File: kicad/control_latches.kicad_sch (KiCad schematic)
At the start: 5 parts, among them U11 7406, U6 74LS374, U7 74LS374, U8 74LS04, U9 74LS08

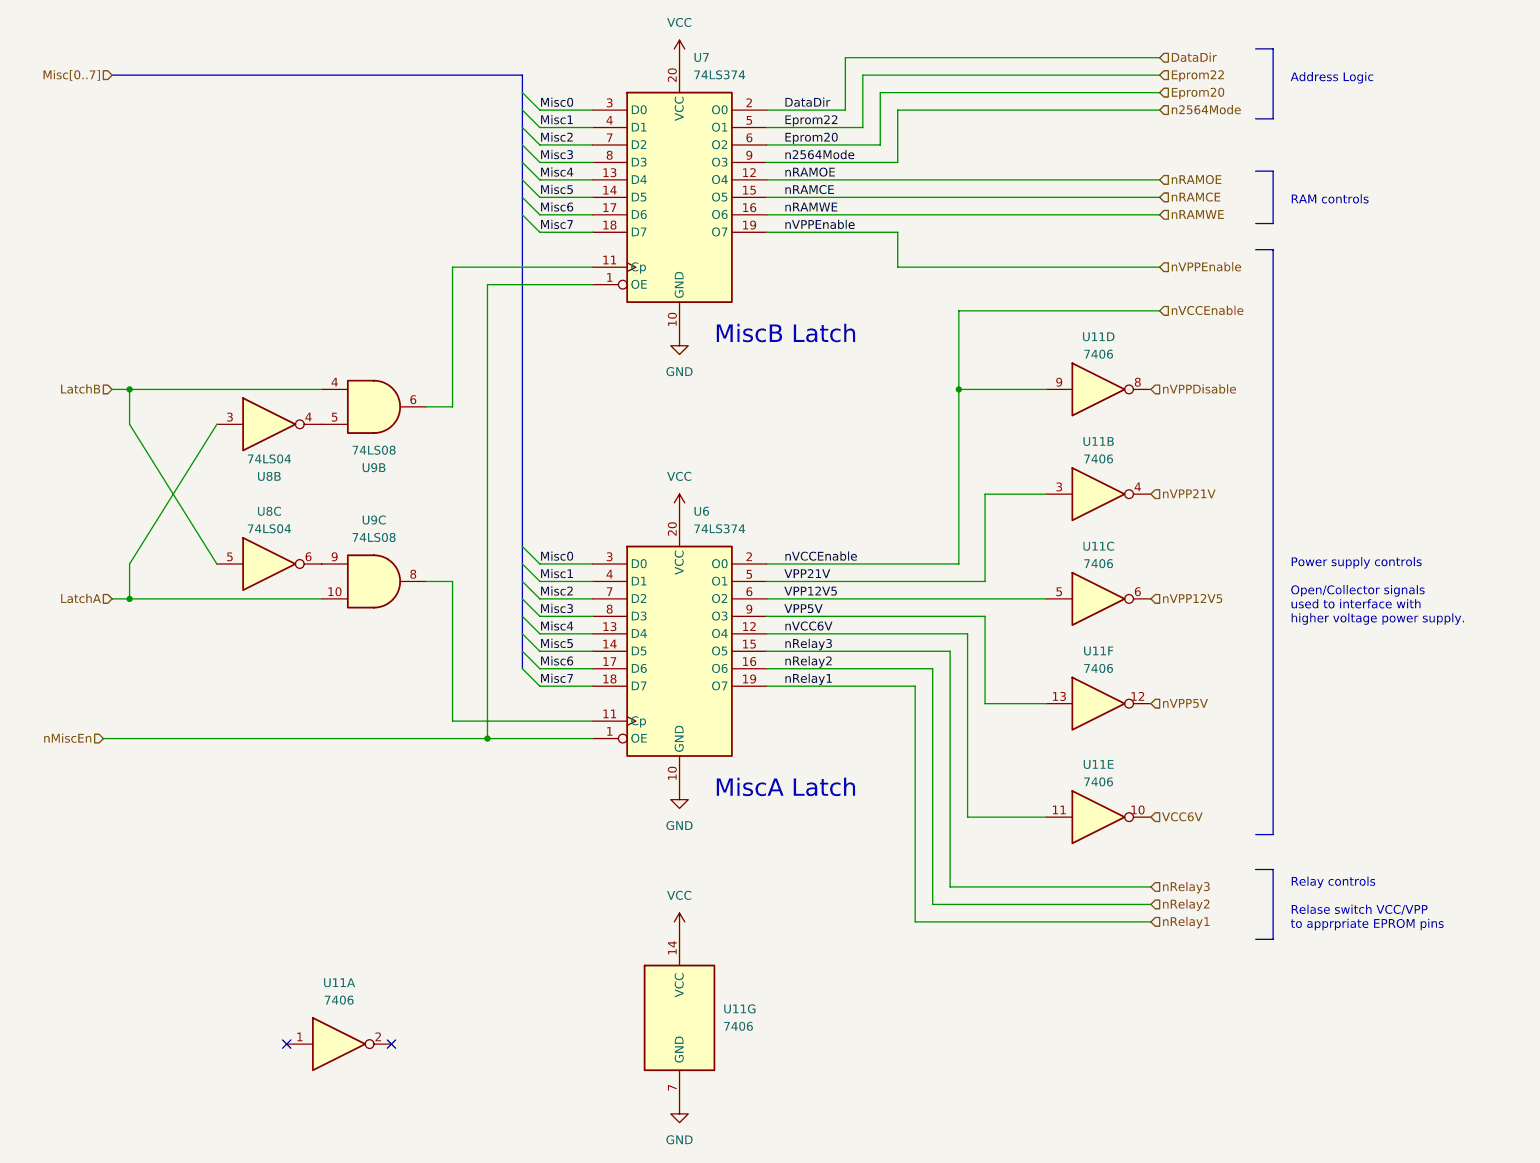
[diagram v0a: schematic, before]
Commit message: Move 7406 onto PSU sheet
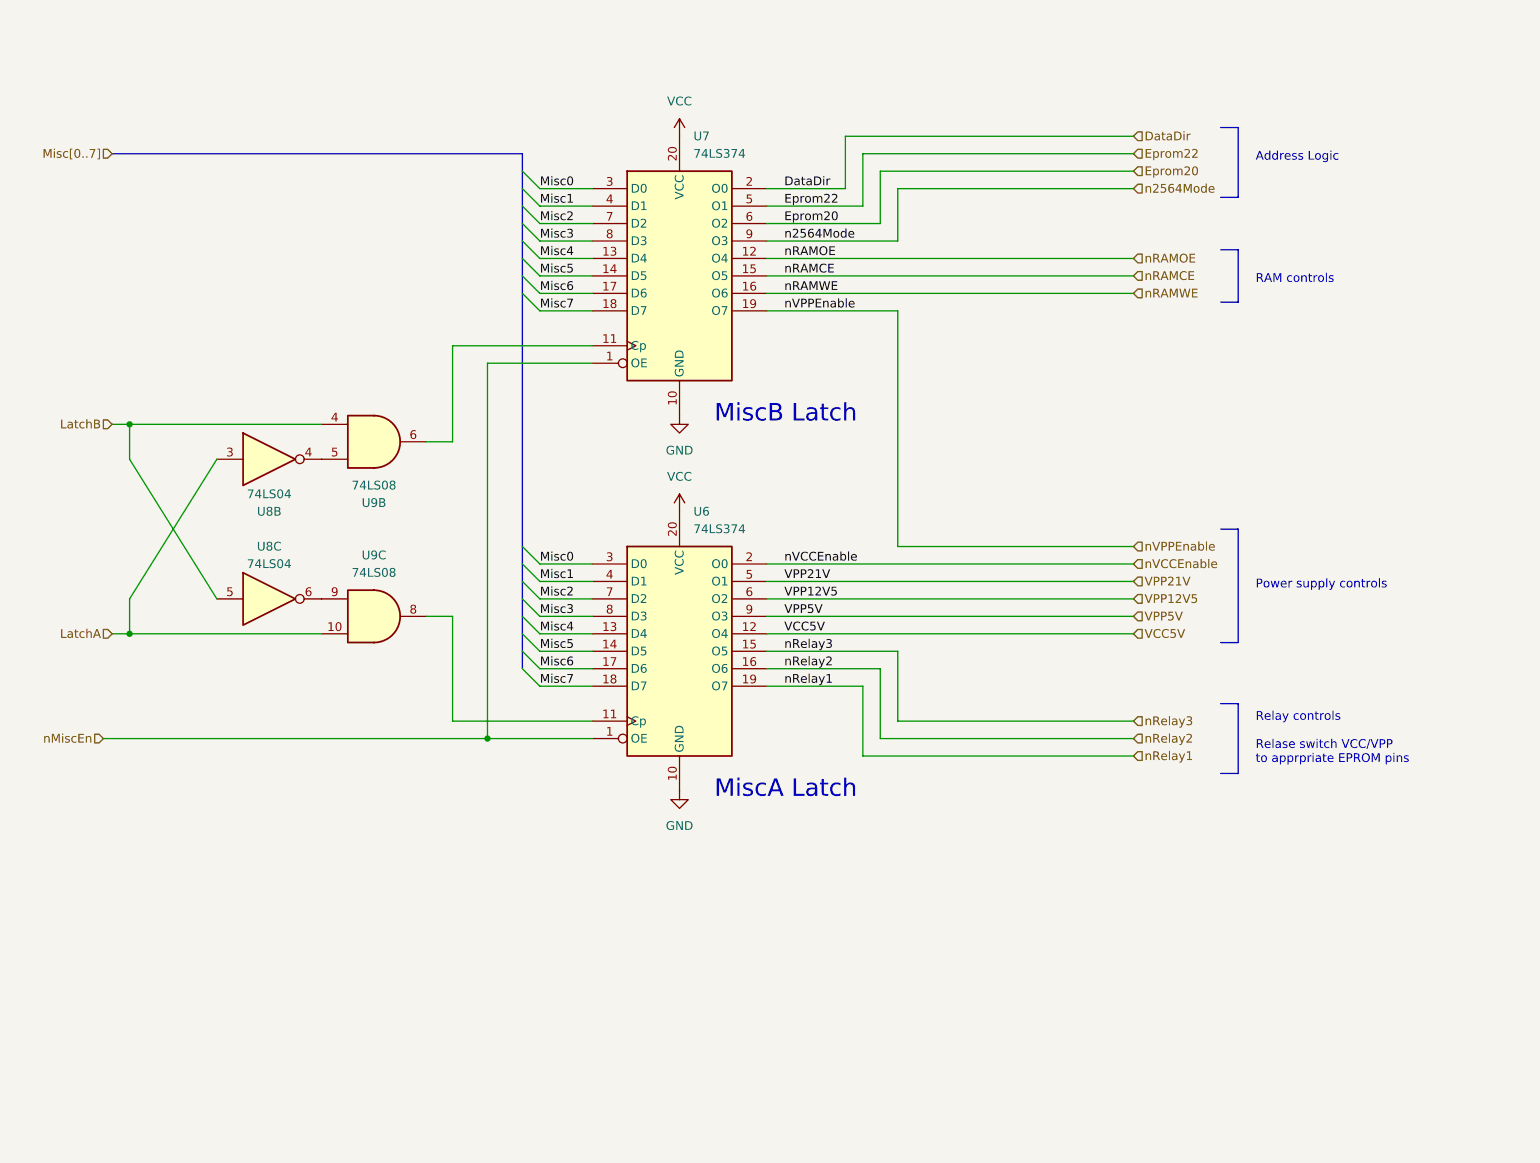
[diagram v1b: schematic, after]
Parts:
- removed U11: 7406, symbol 74xx:74LS06
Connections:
- net nVCC6V renamed VCC5V
- no-connect marks 2 -> 0
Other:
- note added: "Power supply controls"
- note removed: "Power supply controls Open/Collector signals used to interface with higher voltage power supply."
- moved on the sheet: U7, U8B, U8C, U9B, U9C

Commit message: KiCAD: Initial PCB placement
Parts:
- U6, U7: footprint (none) -> Package_DIP:DIP-20_W7.62mm_LongPads
- U8, U9: footprint (none) -> Package_DIP:DIP-14_W7.62mm_LongPads
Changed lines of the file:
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@@
     (property "Reference" "U8" (id 0) (at 90.17 97.79 0))
     (property "Value" "74LS04" (id 1) (at 90.17 100.33 0))
-    (property "Footprint" "" (id 2) (at 90.17 105.41 0)
+    (property "Footprint" "Package_DIP:DIP-14_W7.62mm_LongPads" (id 2) (at 90.17 105.41 0)
       (effects (font (size 1.27 1.27)) hide)
     )
@@
     (property "Reference" "U9" (id 0) (at 105.41 99.06 0))
     (property "Value" "74LS08" (id 1) (at 105.41 101.6 0))
-    (property "Footprint" "" (id 2) (at 105.41 107.95 0)
+    (property "Footprint" "Package_DIP:DIP-14_W7.62mm_LongPads" (id 2) (at 105.41 107.95 0)
       (effects (font (size 1.27 1.27)) hide)
     )
@@
     (property "Reference" "U8" (id 0) (at 90.17 92.71 0))
     (property "Value" "74LS04" (id 1) (at 90.17 90.17 0))
-    (property "Footprint" "" (id 2) (at 90.17 85.09 0)
+    (property "Footprint" "Package_DIP:DIP-14_W7.62mm_LongPads" (id 2) (at 90.17 85.09 0)
       (effects (font (size 1.27 1.27)) hide)
     )
@@
     (property "Reference" "U9" (id 0) (at 105.41 91.44 0))
     (property "Value" "74LS08" (id 1) (at 105.41 88.9 0))
-    (property "Footprint" "" (id 2) (at 105.41 82.55 0)
+    (property "Footprint" "Package_DIP:DIP-14_W7.62mm_LongPads" (id 2) (at 105.41 82.55 0)
       (effects (font (size 1.27 1.27)) hide)
     )
@@
       (effects (font (size 1.27 1.27)) (justify left))
     )
-    (property "Footprint" "" (id 2) (at 149.86 58.42 0)
+    (property "Footprint" "Package_DIP:DIP-20_W7.62mm_LongPads" (id 2) (at 149.86 58.42 0)
       (effects (font (size 1.27 1.27)) hide)
     )
@@
       (effects (font (size 1.27 1.27)) (justify left))
     )
-    (property "Footprint" "" (id 2) (at 149.86 113.03 0)
+    (property "Footprint" "Package_DIP:DIP-20_W7.62mm_LongPads" (id 2) (at 149.86 113.03 0)
       (effects (font (size 1.27 1.27)) hide)
     )

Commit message: KiCAD: PCB now routed
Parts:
- U6, U7: footprint Package_DIP:DIP-20_W7.62mm_LongPads -> Package_DIP:DIP-20_W7.62mm
- U8, U9: footprint Package_DIP:DIP-14_W7.62mm_LongPads -> Package_DIP:DIP-14_W7.62mm
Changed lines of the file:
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@@
     (property "Reference" "U8" (id 0) (at 90.17 97.79 0))
     (property "Value" "74LS04" (id 1) (at 90.17 100.33 0))
-    (property "Footprint" "Package_DIP:DIP-14_W7.62mm_LongPads" (id 2) (at 90.17 105.41 0)
+    (property "Footprint" "Package_DIP:DIP-14_W7.62mm" (id 2) (at 90.17 105.41 0)
       (effects (font (size 1.27 1.27)) hide)
     )
@@
     (property "Reference" "U9" (id 0) (at 105.41 99.06 0))
     (property "Value" "74LS08" (id 1) (at 105.41 101.6 0))
-    (property "Footprint" "Package_DIP:DIP-14_W7.62mm_LongPads" (id 2) (at 105.41 107.95 0)
+    (property "Footprint" "Package_DIP:DIP-14_W7.62mm" (id 2) (at 105.41 107.95 0)
       (effects (font (size 1.27 1.27)) hide)
     )
@@
     (property "Reference" "U8" (id 0) (at 90.17 92.71 0))
     (property "Value" "74LS04" (id 1) (at 90.17 90.17 0))
-    (property "Footprint" "Package_DIP:DIP-14_W7.62mm_LongPads" (id 2) (at 90.17 85.09 0)
+    (property "Footprint" "Package_DIP:DIP-14_W7.62mm" (id 2) (at 90.17 85.09 0)
       (effects (font (size 1.27 1.27)) hide)
     )
@@
     (property "Reference" "U9" (id 0) (at 105.41 91.44 0))
     (property "Value" "74LS08" (id 1) (at 105.41 88.9 0))
-    (property "Footprint" "Package_DIP:DIP-14_W7.62mm_LongPads" (id 2) (at 105.41 82.55 0)
+    (property "Footprint" "Package_DIP:DIP-14_W7.62mm" (id 2) (at 105.41 82.55 0)
       (effects (font (size 1.27 1.27)) hide)
     )
@@
       (effects (font (size 1.27 1.27)) (justify left))
     )
-    (property "Footprint" "Package_DIP:DIP-20_W7.62mm_LongPads" (id 2) (at 149.86 58.42 0)
+    (property "Footprint" "Package_DIP:DIP-20_W7.62mm" (id 2) (at 149.86 58.42 0)
       (effects (font (size 1.27 1.27)) hide)
     )
@@
       (effects (font (size 1.27 1.27)) (justify left))
     )
-    (property "Footprint" "Package_DIP:DIP-20_W7.62mm_LongPads" (id 2) (at 149.86 113.03 0)
+    (property "Footprint" "Package_DIP:DIP-20_W7.62mm" (id 2) (at 149.86 113.03 0)
       (effects (font (size 1.27 1.27)) hide)
     )

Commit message: KiCAD - more silk screen
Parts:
- U6, U7: footprint Package_DIP:DIP-20_W7.62mm -> Package_DIP:DIP-20_W7.62mm_Socket
- U8, U9: footprint Package_DIP:DIP-14_W7.62mm -> Package_DIP:DIP-14_W7.62mm_Socket
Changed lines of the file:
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@@
     (property "Reference" "U8" (id 0) (at 90.17 97.79 0))
     (property "Value" "74LS04" (id 1) (at 90.17 100.33 0))
-    (property "Footprint" "Package_DIP:DIP-14_W7.62mm" (id 2) (at 90.17 105.41 0)
+    (property "Footprint" "Package_DIP:DIP-14_W7.62mm_Socket" (id 2) (at 90.17 105.41 0)
       (effects (font (size 1.27 1.27)) hide)
     )
@@
     (property "Reference" "U9" (id 0) (at 105.41 99.06 0))
     (property "Value" "74LS08" (id 1) (at 105.41 101.6 0))
-    (property "Footprint" "Package_DIP:DIP-14_W7.62mm" (id 2) (at 105.41 107.95 0)
+    (property "Footprint" "Package_DIP:DIP-14_W7.62mm_Socket" (id 2) (at 105.41 107.95 0)
       (effects (font (size 1.27 1.27)) hide)
     )
@@
     (property "Reference" "U8" (id 0) (at 90.17 92.71 0))
     (property "Value" "74LS04" (id 1) (at 90.17 90.17 0))
-    (property "Footprint" "Package_DIP:DIP-14_W7.62mm" (id 2) (at 90.17 85.09 0)
+    (property "Footprint" "Package_DIP:DIP-14_W7.62mm_Socket" (id 2) (at 90.17 85.09 0)
       (effects (font (size 1.27 1.27)) hide)
     )
@@
     (property "Reference" "U9" (id 0) (at 105.41 91.44 0))
     (property "Value" "74LS08" (id 1) (at 105.41 88.9 0))
-    (property "Footprint" "Package_DIP:DIP-14_W7.62mm" (id 2) (at 105.41 82.55 0)
+    (property "Footprint" "Package_DIP:DIP-14_W7.62mm_Socket" (id 2) (at 105.41 82.55 0)
       (effects (font (size 1.27 1.27)) hide)
     )
@@
       (effects (font (size 1.27 1.27)) (justify left))
     )
-    (property "Footprint" "Package_DIP:DIP-20_W7.62mm" (id 2) (at 149.86 58.42 0)
+    (property "Footprint" "Package_DIP:DIP-20_W7.62mm_Socket" (id 2) (at 149.86 58.42 0)
       (effects (font (size 1.27 1.27)) hide)
     )
@@
       (effects (font (size 1.27 1.27)) (justify left))
     )
-    (property "Footprint" "Package_DIP:DIP-20_W7.62mm" (id 2) (at 149.86 113.03 0)
+    (property "Footprint" "Package_DIP:DIP-20_W7.62mm_Socket" (id 2) (at 149.86 113.03 0)
       (effects (font (size 1.27 1.27)) hide)
     )

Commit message: KiCAD: Customize IC footprint silk screen
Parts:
- U6, U7: footprint Package_DIP:DIP-20_W7.62mm_Socket -> custom_footprints:DIP-20_W7.62mm_Socket
- U8, U9: footprint Package_DIP:DIP-14_W7.62mm_Socket -> custom_footprints:DIP-14_W7.62mm_Socket
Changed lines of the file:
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@@
     (property "Reference" "U8" (id 0) (at 90.17 97.79 0))
     (property "Value" "74LS04" (id 1) (at 90.17 100.33 0))
-    (property "Footprint" "Package_DIP:DIP-14_W7.62mm_Socket" (id 2) (at 90.17 105.41 0)
+    (property "Footprint" "custom_footprints:DIP-14_W7.62mm_Socket" (id 2) (at 90.17 105.41 0)
       (effects (font (size 1.27 1.27)) hide)
     )
@@
     (property "Reference" "U9" (id 0) (at 105.41 99.06 0))
     (property "Value" "74LS08" (id 1) (at 105.41 101.6 0))
-    (property "Footprint" "Package_DIP:DIP-14_W7.62mm_Socket" (id 2) (at 105.41 107.95 0)
+    (property "Footprint" "custom_footprints:DIP-14_W7.62mm_Socket" (id 2) (at 105.41 107.95 0)
       (effects (font (size 1.27 1.27)) hide)
     )
@@
     (property "Reference" "U8" (id 0) (at 90.17 92.71 0))
     (property "Value" "74LS04" (id 1) (at 90.17 90.17 0))
-    (property "Footprint" "Package_DIP:DIP-14_W7.62mm_Socket" (id 2) (at 90.17 85.09 0)
+    (property "Footprint" "custom_footprints:DIP-14_W7.62mm_Socket" (id 2) (at 90.17 85.09 0)
       (effects (font (size 1.27 1.27)) hide)
     )
@@
     (property "Reference" "U9" (id 0) (at 105.41 91.44 0))
     (property "Value" "74LS08" (id 1) (at 105.41 88.9 0))
-    (property "Footprint" "Package_DIP:DIP-14_W7.62mm_Socket" (id 2) (at 105.41 82.55 0)
+    (property "Footprint" "custom_footprints:DIP-14_W7.62mm_Socket" (id 2) (at 105.41 82.55 0)
       (effects (font (size 1.27 1.27)) hide)
     )
@@
       (effects (font (size 1.27 1.27)) (justify left))
     )
-    (property "Footprint" "Package_DIP:DIP-20_W7.62mm_Socket" (id 2) (at 149.86 58.42 0)
+    (property "Footprint" "custom_footprints:DIP-20_W7.62mm_Socket" (id 2) (at 149.86 58.42 0)
       (effects (font (size 1.27 1.27)) hide)
     )
@@
       (effects (font (size 1.27 1.27)) (justify left))
     )
-    (property "Footprint" "Package_DIP:DIP-20_W7.62mm_Socket" (id 2) (at 149.86 113.03 0)
+    (property "Footprint" "custom_footprints:DIP-20_W7.62mm_Socket" (id 2) (at 149.86 113.03 0)
       (effects (font (size 1.27 1.27)) hide)
     )
